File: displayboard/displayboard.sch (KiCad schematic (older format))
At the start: 5 parts, among them P1 CONN_01X08, P2 CONN_01X08

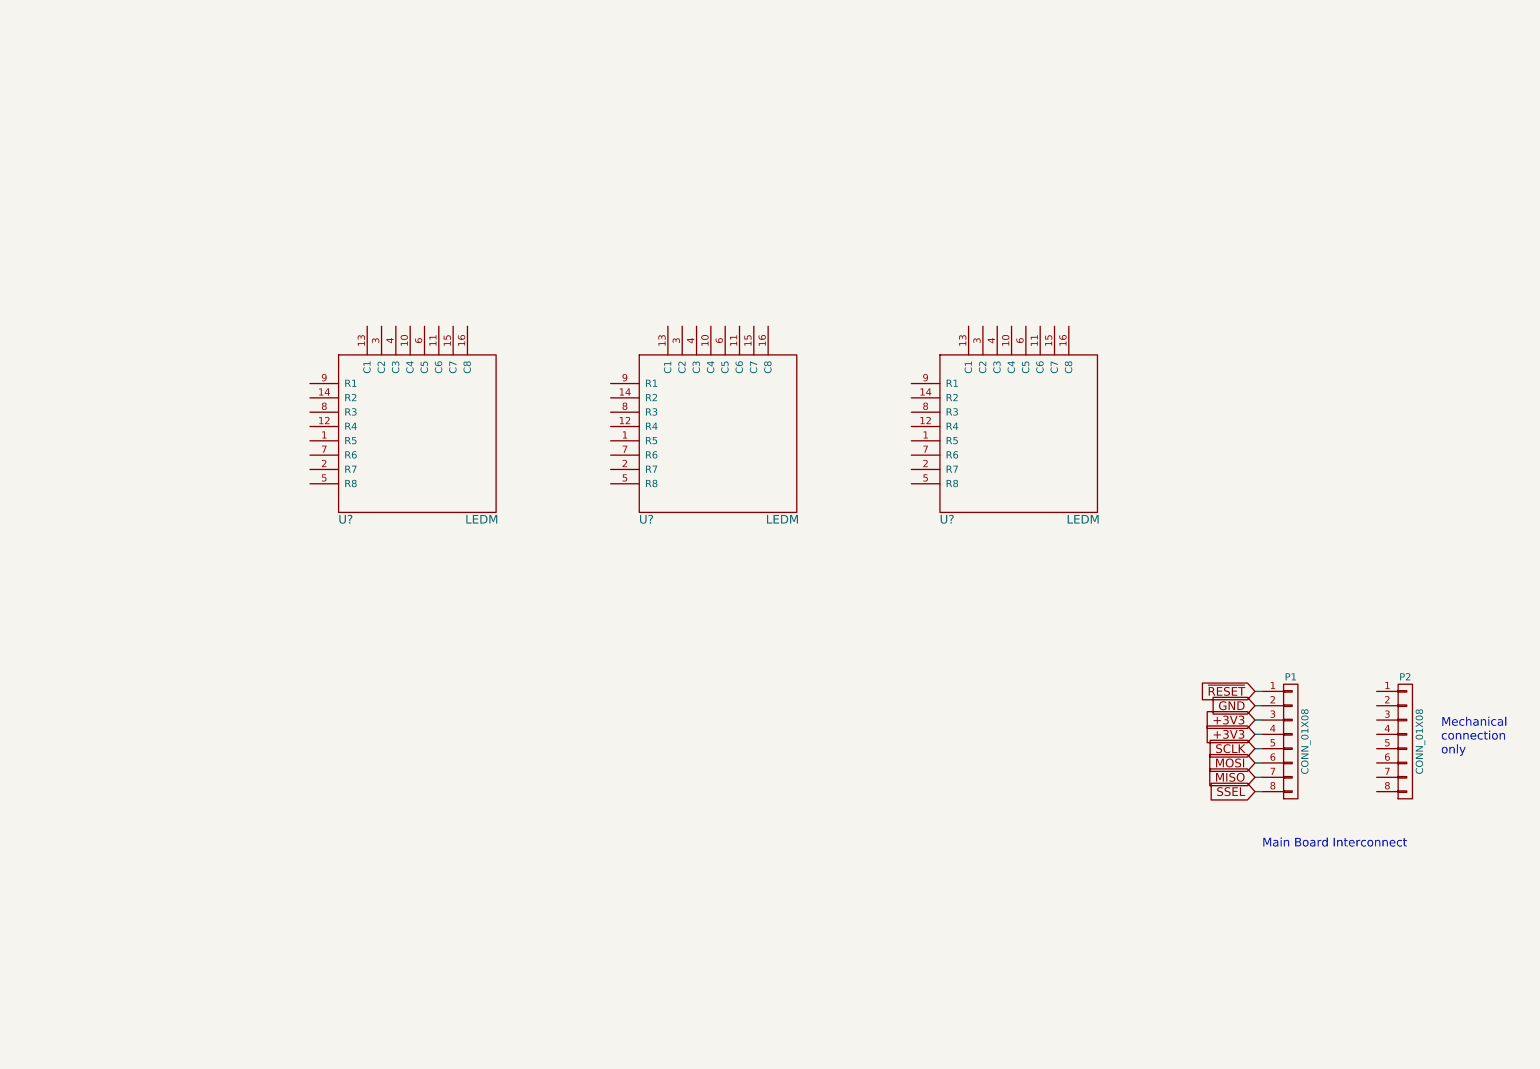
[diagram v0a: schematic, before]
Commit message: MAX6960 schematic symbol.
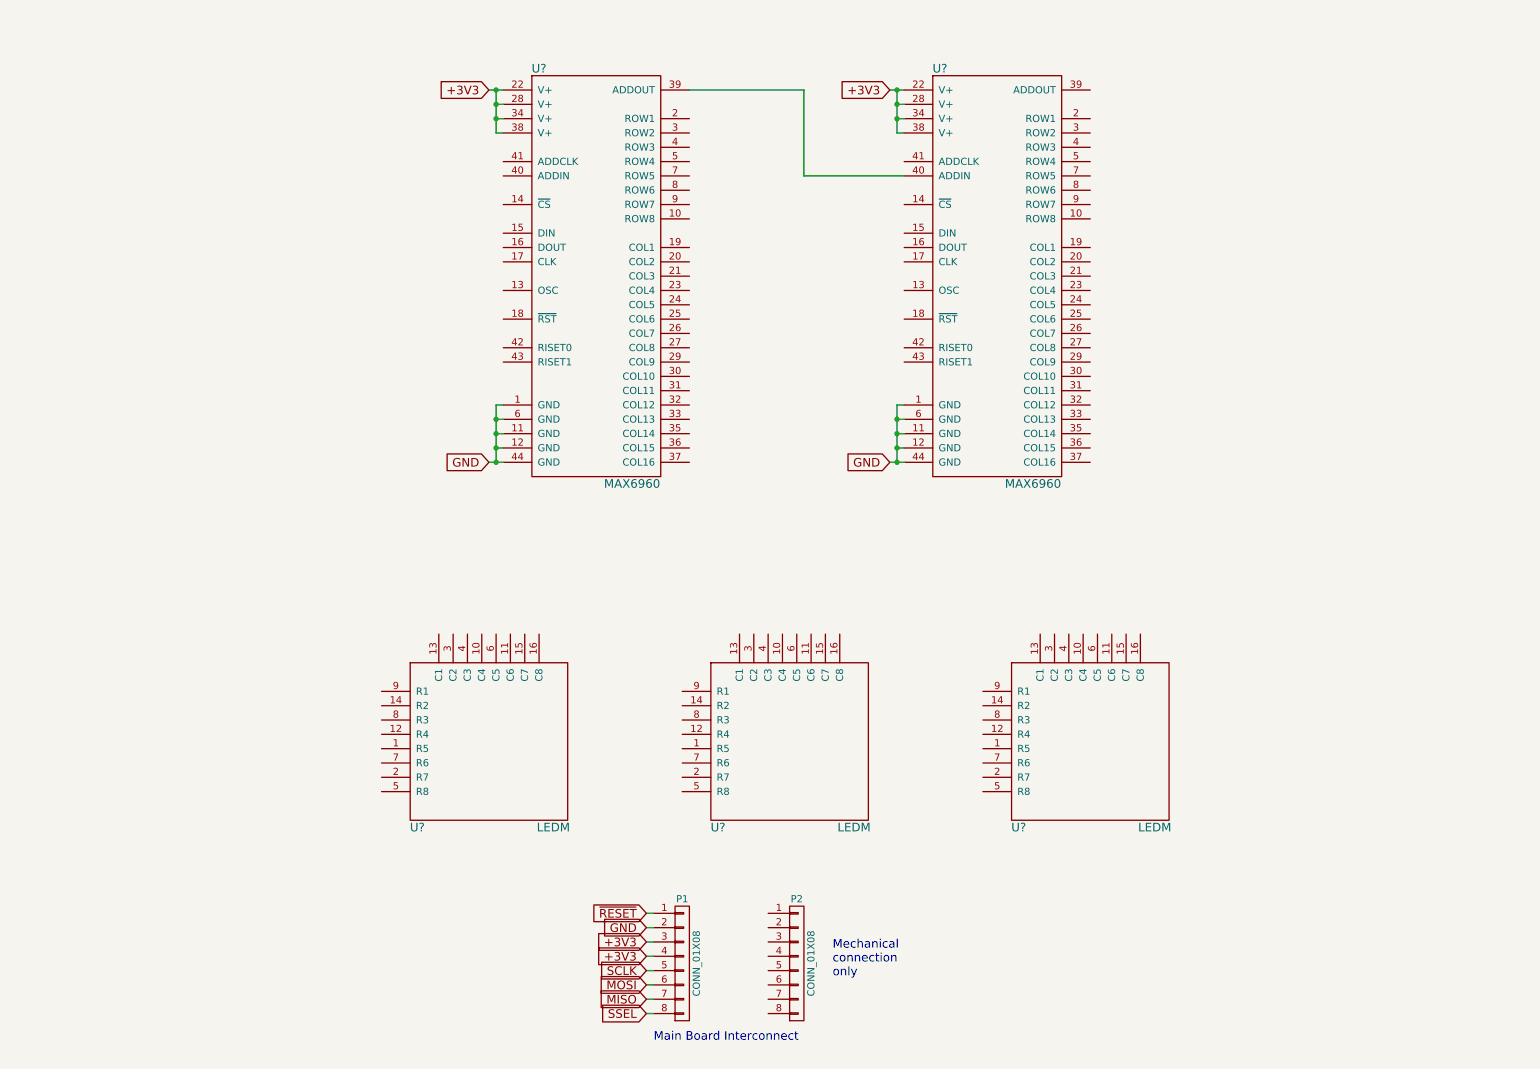
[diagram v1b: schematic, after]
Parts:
- added U? (x2): MAX6960, symbol MAX6960
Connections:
- net +3V3: now also U?.22 (V+), U?.22 (V+), U?.28 (V+), U?.28 (V+), U?.34 (V+), U?.34 (V+), U?.38 (V+), U?.38 (V+)
- net GND: now also U?.1 (GND), U?.1 (GND), U?.11 (GND), U?.11 (GND), U?.12 (GND), U?.12 (GND), U?.44 (GND), U?.44 (GND), U?.6 (GND), U?.6 (GND)
- new net: U?.39 (ADDOUT), U?.40 (ADDIN)
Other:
- moved on the sheet: P1, P2, U?
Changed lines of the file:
@@
 L CONN_01X08 P1
 U 1 1 55EE8B80
-P 9450 5650
-F 0 "P1" H 9450 6100 50  0000 C CNN
-F 1 "CONN_01X08" V 9550 5650 50  0000 C CNN
-F 2 "Pin_Headers:Pin_Header_Straight_1x08" H 9450 5650 60  0001 C CNN
-F 3 "" H 9450 5650 60  0000 C CNN
-	1    9450 5650
+P 5200 7200
+F 0 "P1" H 5200 7650 50  0000 C CNN
+F 1 "CONN_01X08" V 5300 7200 50  0000 C CNN
+F 2 "Pin_Headers:Pin_Header_Straight_1x08" H 5200 7200 60  0001 C CNN
+F 3 "" H 5200 7200 60  0000 C CNN
+	1    5200 7200
 	1    0    0    -1
 $EndComp
@@
 L CONN_01X08 P2
 U 1 1 55EE8C35
-P 10250 5650
-F 0 "P2" H 10250 6100 50  0000 C CNN
-F 1 "CONN_01X08" V 10350 5650 50  0000 C CNN
-F 2 "Pin_Headers:Pin_Header_Straight_1x08" H 10250 5650 60  0001 C CNN
-F 3 "" H 10250 5650 60  0000 C CNN
-	1    10250 5650
+P 6000 7200
+F 0 "P2" H 6000 7650 50  0000 C CNN
+F 1 "CONN_01X08" V 6100 7200 50  0000 C CNN
+F 2 "Pin_Headers:Pin_Header_Straight_1x08" H 6000 7200 60  0001 C CNN
+F 3 "" H 6000 7200 60  0000 C CNN
+	1    6000 7200
 	1    0    0    -1
 $EndComp
-Text Notes 10500 5750 0    60   ~ 0
+Text Notes 6250 7300 0    60   ~ 0
 Mechanical\nconnection\nonly
-Text GLabel 9200 5400 0    60   Input ~ 0
+Text GLabel 4950 6950 0    60   Input ~ 0
 GND
-Text GLabel 9200 5500 0    60   Input ~ 0
+Text GLabel 4950 7050 0    60   Input ~ 0
 +3V3
-Text GLabel 9200 5600 0    60   Input ~ 0
+Text GLabel 4950 7150 0    60   Input ~ 0
 +3V3
-Text GLabel 9200 5700 0    60   Input ~ 0
+Text GLabel 4950 7250 0    60   Input ~ 0
 SCLK
-Text GLabel 9200 5800 0    60   Input ~ 0
+Text GLabel 4950 7350 0    60   Input ~ 0
 MOSI
-Text GLabel 9200 5900 0    60   Input ~ 0
+Text GLabel 4950 7450 0    60   Input ~ 0
 MISO
-Text GLabel 9200 6000 0    60   Input ~ 0
+Text GLabel 4950 7550 0    60   Input ~ 0
 SSEL
-Text GLabel 9200 5300 0    60   Input ~ 0
+Text GLabel 4950 6850 0    60   Input ~ 0
 ~RESET
 Wire Wire Line
-	9200 5300 9250 5300
+	4950 6850 5000 6850
 Wire Wire Line
-	9200 5400 9250 5400
+	4950 6950 5000 6950
 Wire Wire Line
-	9200 5500 9250 5500
+	4950 7050 5000 7050
 Wire Wire Line
-	9200 5600 9250 5600
+	4950 7150 5000 7150
 Wire Wire Line
-	9200 5700 9250 5700
+	4950 7250 5000 7250
 Wire Wire Line
-	9200 5800 9250 5800
+	4950 7350 5000 7350
 Wire Wire Line
-	9200 5900 9250 5900
+	4950 7450 5000 7450
 Wire Wire Line
-	9200 6000 9250 6000
-Text Notes 9250 6400 0    60   ~ 0
+	4950 7550 5000 7550
+Text Notes 5000 7750 0    60   ~ 0
 Main Board Interconnect
 $Comp
 L LEDM U?
 U 1 1 56526517
-P 3350 3500
-F 0 "U?" H 2850 2900 60  0000 C CNN
-F 1 "LEDM" H 3800 2900 60  0000 C CNN
-F 2 "" H 3200 3500 60  0000 C CNN
-F 3 "" H 3200 3500 60  0000 C CNN
-	1    3350 3500
+P 3850 5650
+F 0 "U?" H 3350 5050 60  0000 C CNN
+F 1 "LEDM" H 4300 5050 60  0000 C CNN
+F 2 "" H 3700 5650 60  0000 C CNN
+F 3 "" H 3700 5650 60  0000 C CNN
+	1    3850 5650
 	1    0    0    -1
 $EndComp
@@
 L LEDM U?
 U 1 1 56526560
-P 5450 3500
-F 0 "U?" H 4950 2900 60  0000 C CNN
-F 1 "LEDM" H 5900 2900 60  0000 C CNN
-F 2 "" H 5300 3500 60  0000 C CNN
-F 3 "" H 5300 3500 60  0000 C CNN
-	1    5450 3500
+P 5950 5650
+F 0 "U?" H 5450 5050 60  0000 C CNN
+F 1 "LEDM" H 6400 5050 60  0000 C CNN
+F 2 "" H 5800 5650 60  0000 C CNN
+F 3 "" H 5800 5650 60  0000 C CNN
+	1    5950 5650
 	1    0    0    -1
 $EndComp
@@
 L LEDM U?
 U 1 1 565265E7
-P 7550 3500
-F 0 "U?" H 7050 2900 60  0000 C CNN
-F 1 "LEDM" H 8000 2900 60  0000 C CNN
-F 2 "" H 7400 3500 60  0000 C CNN
-F 3 "" H 7400 3500 60  0000 C CNN
-	1    7550 3500
+P 8050 5650
+F 0 "U?" H 7550 5050 60  0000 C CNN
+F 1 "LEDM" H 8500 5050 60  0000 C CNN
+F 2 "" H 7900 5650 60  0000 C CNN
+F 3 "" H 7900 5650 60  0000 C CNN
+	1    8050 5650
 	1    0    0    -1
 $EndComp
+$Comp
+L MAX6960 U?
+U 1 1 56527C95
+P 4600 2350
+F 0 "U?" H 4200 3750 60  0000 C CNN
+F 1 "MAX6960" H 4850 850 60  0000 C CNN
+F 2 "" H 4400 1350 60  0000 C CNN
+F 3 "" H 4400 1350 60  0000 C CNN
+	1    4600 2350
+	1    0    0    -1
+$EndComp
+$Comp
+L MAX6960 U?
+U 1 1 56527DE8
+P 7400 2350
+F 0 "U?" H 7000 3750 60  0000 C CNN
+F 1 "MAX6960" H 7650 850 60  0000 C CNN
+F 2 "" H 7200 1350 60  0000 C CNN
+F 3 "" H 7200 1350 60  0000 C CNN
+	1    7400 2350
+	1    0    0    -1
+$EndComp
+Text GLabel 6650 1100 0    60   Input ~ 0
++3V3
+Wire Wire Line
+	6650 1100 6750 1100
+Wire Wire Line
+	6700 1100 6700 1400
+Wire Wire Line
+	6700 1200 6750 1200
+Connection ~ 6700 1100
+Wire Wire Line
+	6700 1300 6750 1300
+Connection ~ 6700 1200
+Wire Wire Line
+	6700 1400 6750 1400
+Connection ~ 6700 1300
+Text GLabel 3850 1100 0    60   Input ~ 0
++3V3
+Wire Wire Line
+	3850 1100 3950 1100
+Wire Wire Line
+	3900 1100 3900 1400
+Wire Wire Line
+	3900 1200 3950 1200
+Connection ~ 3900 1100
+Wire Wire Line
+	3900 1300 3950 1300
+Connection ~ 3900 1200
+Wire Wire Line
+	3900 1400 3950 1400
+Connection ~ 3900 1300
+Text GLabel 3850 3700 0    60   Input ~ 0
+GND
+Wire Wire Line
+	3850 3700 3950 3700
+Wire Wire Line
+	3900 3300 3900 3700
+Wire Wire Line
+	3900 3600 3950 3600
+Connection ~ 3900 3700
+Wire Wire Line
+	3900 3500 3950 3500
+Connection ~ 3900 3600
+Wire Wire Line
+	3900 3400 3950 3400
+Connection ~ 3900 3500
+Wire Wire Line
+	3900 3300 3950 3300
+Connection ~ 3900 3400
+Text GLabel 6650 3700 0    60   Input ~ 0
+GND
+Wire Wire Line
+	6650 3700 6750 3700
+Wire Wire Line
+	6700 3300 6700 3700
+Wire Wire Line
+	6700 3600 6750 3600
+Connection ~ 6700 3700
+Wire Wire Line
+	6700 3500 6750 3500
+Connection ~ 6700 3600
+Wire Wire Line
+	6700 3400 6750 3400
+Connection ~ 6700 3500
+Wire Wire Line
+	6700 3300 6750 3300
+Connection ~ 6700 3400
+Wire Wire Line
+	5250 1100 6050 1100
+Wire Wire Line
+	6050 1100 6050 1700
+Wire Wire Line
+	6050 1700 6750 1700
 $EndSCHEMATC

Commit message: Complete schematic.
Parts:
- added C1, C10, C2, C3, C4, C5, C7, C8, C9: 0.1u, symbol C_Small
- added C11, C6: 47uF, symbol CP_Small
- added JP1, JP2, JP3, JP4: Jumper_NO_Small, symbol Jumper_NO_Small
- added U1: SG-636PCE, symbol SG-636PCE
- added W1: RED, symbol TEST
- added W2: BLK, symbol TEST
- added W3, W6: BLU, symbol TEST
- added W4, W5: GRN, symbol TEST
- gave numbers to parts that had none: 5
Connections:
- net +3V3: now also U3.40 (ADDIN), C1.1, C10.1, C11.1, C2.1, C3.1, C4.1, C5.1, C6.1, C7.1, C8.1, C9.1, U1.4 (VCC), W1.1; no longer P1.3 (P3)
- net GND: now also C1.2, C10.2, C11.2, C2.2, C3.2, C4.2, C5.2, C6.2, C7.2, C8.2, C9.2, JP1.1, JP2.2, JP3.1, JP4.2, U1.2 (GND), W2.1; no longer P1.2 (P2)
- net MISO: now also U3.16 (DOUT), U5.16 (DOUT); no longer P1.7 (P7)
- net MOSI: now also U3.15 (DIN), U5.15 (DIN); no longer P1.6 (P6)
- net SCLK: now also U3.17 (CLK), U5.17 (CLK); no longer P1.5 (P5)
- net SSEL: now also U3.14 (~CS), U5.14 (~CS); no longer P1.8 (P8)
- net ~RESET: now also U3.18 (~RST), U5.18 (~RST)
- net D0_R5: now reaches U2.1 (R5)
- net D0_R5: now also U3.7 (ROW5), U4.1 (R5)
- net D0_C4: now reaches U2.10 (C4)
- net D0_C4: now also U3.23 (COL4)
- net D0_C6: now reaches U2.11 (C6)
- net D0_C6: now also U3.25 (COL6)
- net D0_R4: now reaches U2.12 (R4)
- net D0_R4: now also U3.5 (ROW4), U4.12 (R4)
- net D0_C1: now reaches U2.13 (C1)
- net D0_C1: now also U3.19 (COL1)
- net D0_R2: now reaches U2.14 (R2)
- net D0_R2: now also U3.3 (ROW2), U4.14 (R2)
- net D0_C7: now reaches U2.15 (C7)
- net D0_C7: now also U3.26 (COL7)
- net D0_C8: now reaches U2.16 (C8)
- net D0_C8: now also U3.27 (COL8)
- net D0_R7: now reaches U2.2 (R7)
- net D0_R7: now also U3.9 (ROW7), U4.2 (R7)
- net D0_C2: now reaches U2.3 (C2)
- net D0_C2: now also U3.20 (COL2)
- net D0_C3: now reaches U2.4 (C3)
- net D0_C3: now also U3.21 (COL3)
- net D0_R8: now reaches U2.5 (R8)
- net D0_R8: now also U3.10 (ROW8), U4.5 (R8)
- net D0_C5: now reaches U2.6 (C5)
- net D0_C5: now also U3.24 (COL5)
- net D0_R6: now reaches U2.7 (R6)
- net D0_R6: now also U3.8 (ROW6), U4.7 (R6)
- net D0_R3: now reaches U2.8 (R3)
- net D0_R3: now also U3.4 (ROW3), U4.8 (R3)
- net D0_R1: now reaches U2.9 (R1)
- net D0_R1: now also U3.2 (ROW1), U4.9 (R1)
- net D1_C4: now reaches U4.10 (C4)
- net D1_C4: now also U3.32 (COL12)
- net D1_C6: now reaches U4.11 (C6)
- net D1_C6: now also U3.35 (COL14)
- net D1_C1: now reaches U4.13 (C1)
- net D1_C1: now also U3.29 (COL9)
- net D1_C7: now reaches U4.15 (C7)
- net D1_C7: now also U3.36 (COL15)
- net D1_C8: now reaches U4.16 (C8)
- net D1_C8: now also U3.37 (COL16)
- net D1_C2: now reaches U4.3 (C2)
- net D1_C2: now also U3.30 (COL10)
- net D1_C3: now reaches U4.4 (C3)
- net D1_C3: now also U3.31 (COL11)
- net D1_C5: now reaches U4.6 (C5)
- net D1_C5: now also U3.33 (COL13)
- net D2_R5: now reaches U6.1 (R5)
- net D2_R5: now also U5.7 (ROW5)
- net D2_C4: now reaches U6.10 (C4)
- net D2_C4: now also U5.23 (COL4)
- net D2_C6: now reaches U6.11 (C6)
- net D2_C6: now also U5.25 (COL6)
- net D2_R4: now reaches U6.12 (R4)
- net D2_R4: now also U5.5 (ROW4)
- net D2_C1: now reaches U6.13 (C1)
- net D2_C1: now also U5.19 (COL1)
- net D2_R2: now reaches U6.14 (R2)
- net D2_R2: now also U5.3 (ROW2)
- net D2_C7: now reaches U6.15 (C7)
- net D2_C7: now also U5.26 (COL7)
- net D2_C8: now reaches U6.16 (C8)
- net D2_C8: now also U5.27 (COL8)
- net D2_R7: now reaches U6.2 (R7)
- net D2_R7: now also U5.9 (ROW7)
- net D2_C2: now reaches U6.3 (C2)
- net D2_C2: now also U5.20 (COL2)
- net D2_C3: now reaches U6.4 (C3)
- net D2_C3: now also U5.21 (COL3)
- net D2_R8: now reaches U6.5 (R8)
- net D2_R8: now also U5.10 (ROW8)
- net D2_C5: now reaches U6.6 (C5)
- net D2_C5: now also U5.24 (COL5)
- net D2_R6: now reaches U6.7 (R6)
- net D2_R6: now also U5.8 (ROW6)
- net D2_R3: now reaches U6.8 (R3)
- net D2_R3: now also U5.4 (ROW3)
- net D2_R1: now reaches U6.9 (R1)
- net D2_R1: now also U5.2 (ROW1)
- net OSC: now reaches U3.13 (OSC)
- net OSC: now also U5.13 (OSC), U1.3 (OUT)
- net ADDCLK: now reaches U3.41 (ADDCLK)
- net ADDCLK: now also U5.41 (ADDCLK)
- net at U3.42 (RISET0): now also JP1.2
- net at U3.43 (RISET1): now also JP2.1
- net at U5.42 (RISET0): now also JP3.2
- net at U5.43 (RISET1): now also JP4.1
- new net: P1.2 (P2), W2.2
- new net: P1.3 (P3), W1.2
- new net: P1.5 (P5), W3.2
- new net: P1.6 (P6), W4.2
- new net: P1.7 (P7), W5.2
- new net: P1.8 (P8), W6.2
- no-connect marks 0 -> 17
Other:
- note added: "Display Drivers"
- note added: "LED Matrix Displays"
- note added: "Oscillator"
- moved on the sheet: P1, P2, U2, U3, U4, U5, U6
